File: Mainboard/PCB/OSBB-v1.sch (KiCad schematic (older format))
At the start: 30 parts, among them P1 AUX 1-3, P14 EXTRA Pins, P2 Wire to Teensy VUSB, P3 +3.3V, P4 Pit Limiter, P5 Rotary Encoders, P6 BTN 1-32, P7 LED, Q1 NPN, Q2 NPN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

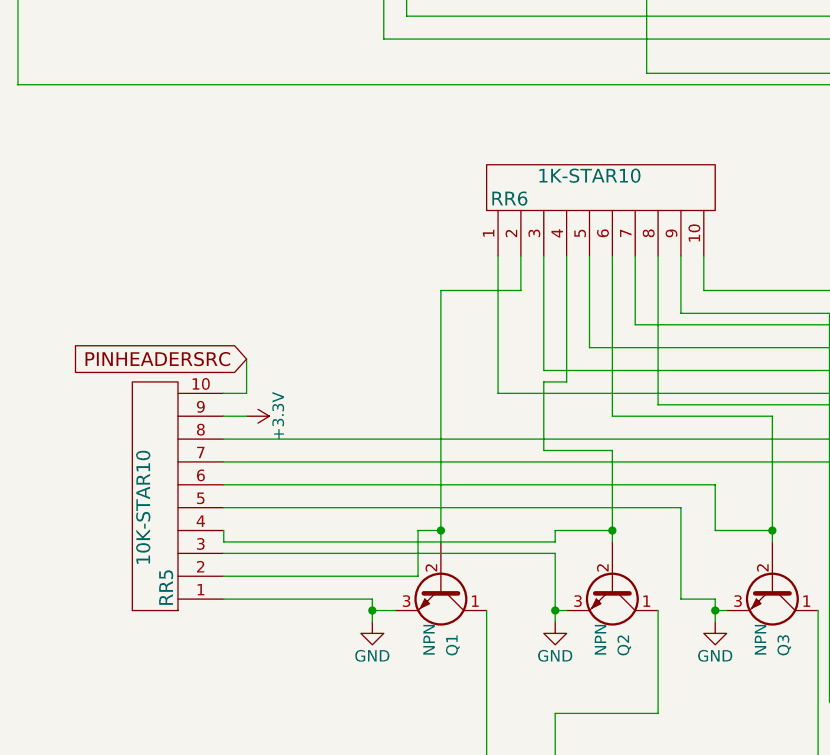
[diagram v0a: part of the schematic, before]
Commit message: * updated schematic for version 1.0   from RC6   * adjusted silkscreen positions   * replaced RR6 and RR5 footprint, removed pin 1 indicator   * C4 now through hole   * removed vias from 32pin supply line
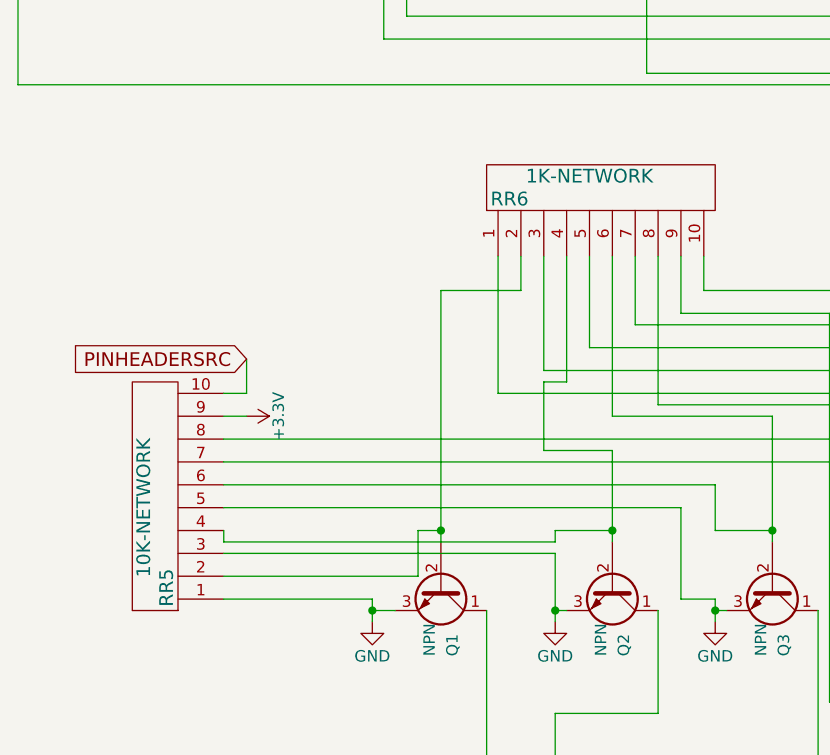
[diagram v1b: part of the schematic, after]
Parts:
- C4: footprint Capacitors_SMD:C_0805_HandSoldering -> Capacitors_ThroughHole:C_Disc_D3.0mm_W2.0mm_P2.50mm
- RR5: value 10K-STAR10 -> 10K-NETWORK; footprint Pin_Headers:Pin_Header_Straight_1x10 -> MOBB-KiCad-Lib:Resistor_Network-1x10
- RR6: value 1K-STAR10 -> 1K-NETWORK; footprint Pin_Headers:Pin_Header_Straight_1x10 -> MOBB-KiCad-Lib:Resistor_Network-1x10
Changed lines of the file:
@@
 LIBS:valves
 LIBS:74hc4051
+LIBS:resistor-star
 LIBS:Teensy3.2
-LIBS:resistor-star
 LIBS:OSBB-v1-cache
 EELAYER 25 0
@@
 F 0 "C4" H 12325 7900 50  0000 L CNN
 F 1 "C" H 12325 7700 50  0000 L CNN
-F 2 "Capacitors_SMD:C_0805_HandSoldering" H 12338 7650 50  0001 C CNN
+F 2 "Capacitors_ThroughHole:C_Disc_D3.0mm_W2.0mm_P2.50mm" H 12338 7650 50  0001 C CNN
 F 3 "" H 12300 7800 50  0000 C CNN
 	1    12300 7800
@@
 P 7450 7950
 F 0 "RR6" H 7100 8200 60  0000 C CNN
-F 1 "1K-STAR10" H 7450 8300 60  0000 C CNN
-F 2 "Pin_Headers:Pin_Header_Straight_1x10" H 7400 7800 60  0001 C CNN
+F 1 "1K-NETWORK" H 7450 8300 60  0000 C CNN
+F 2 "MOBB-KiCad-Lib:Resistor_Network-1x10" H 7400 7800 60  0001 C CNN
 F 3 "" H 7400 7800 60  0001 C CNN
 	1    7450 7950
@@
 P 5850 9050
 F 0 "RR5" H 5500 9300 60  0000 C CNN
-F 1 "10K-STAR10" H 5850 9400 60  0000 C CNN
-F 2 "Pin_Headers:Pin_Header_Straight_1x10" H 5800 8900 60  0001 C CNN
+F 1 "10K-NETWORK" H 5850 9400 60  0000 C CNN
+F 2 "MOBB-KiCad-Lib:Resistor_Network-1x10" H 5800 8900 60  0001 C CNN
 F 3 "" H 5800 8900 60  0001 C CNN
 	1    5850 9050
